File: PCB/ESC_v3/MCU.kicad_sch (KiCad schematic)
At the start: 44 parts, among them J10 Conn_01x01_Pin, J3 Conn_01x01_Pin, J4 Conn_01x01_Pin, J5 Conn_01x01_Pin, J6 Conn_01x01_Pin, J7 Conn_01x01_Pin, J8 Conn_01x01_Pin, J9 Conn_01x01_Pin, U5 STM32G431CBT6, Y2 24MHz

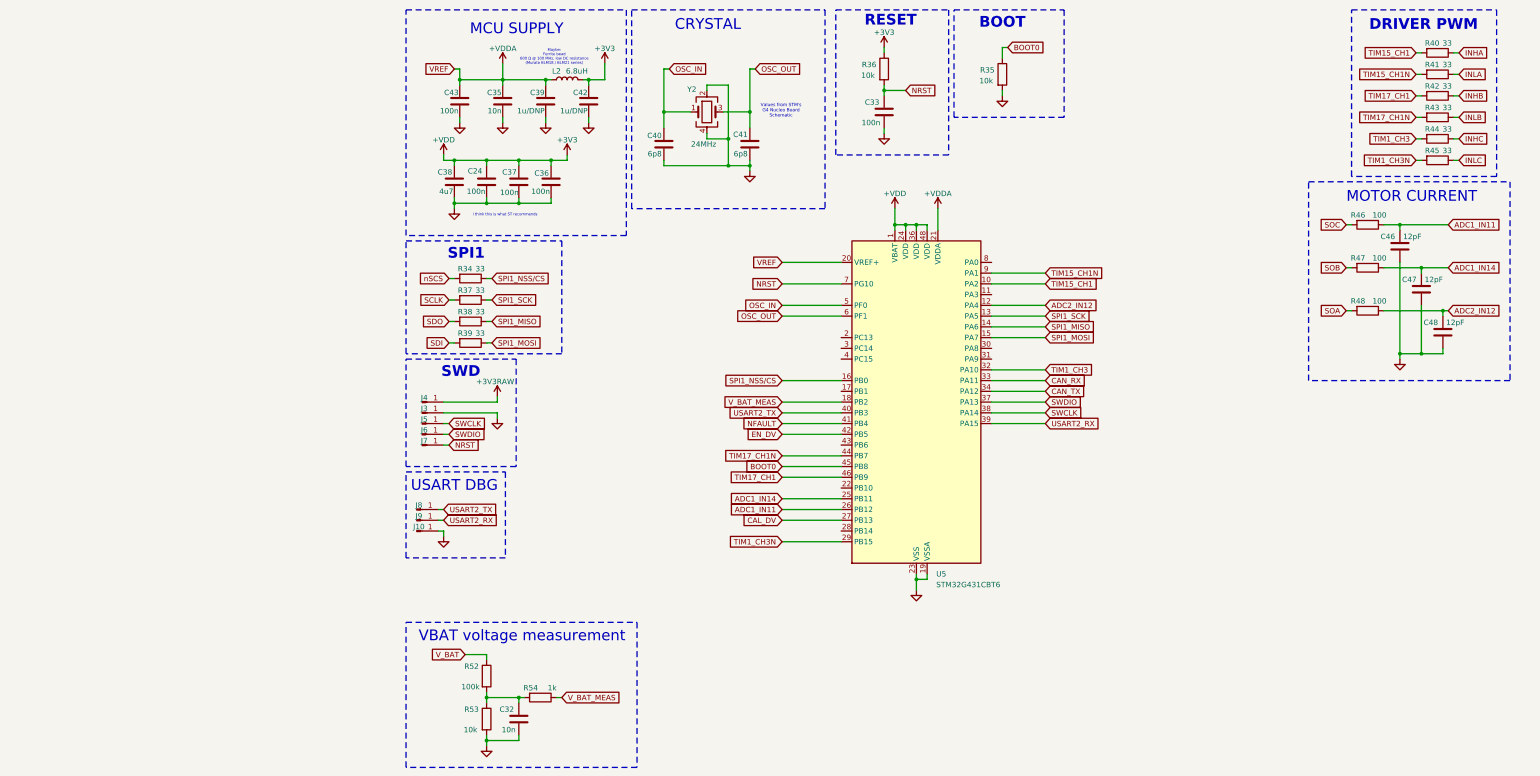
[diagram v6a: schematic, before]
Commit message: STM changed
Changed specific STM model for better pinouts and layout
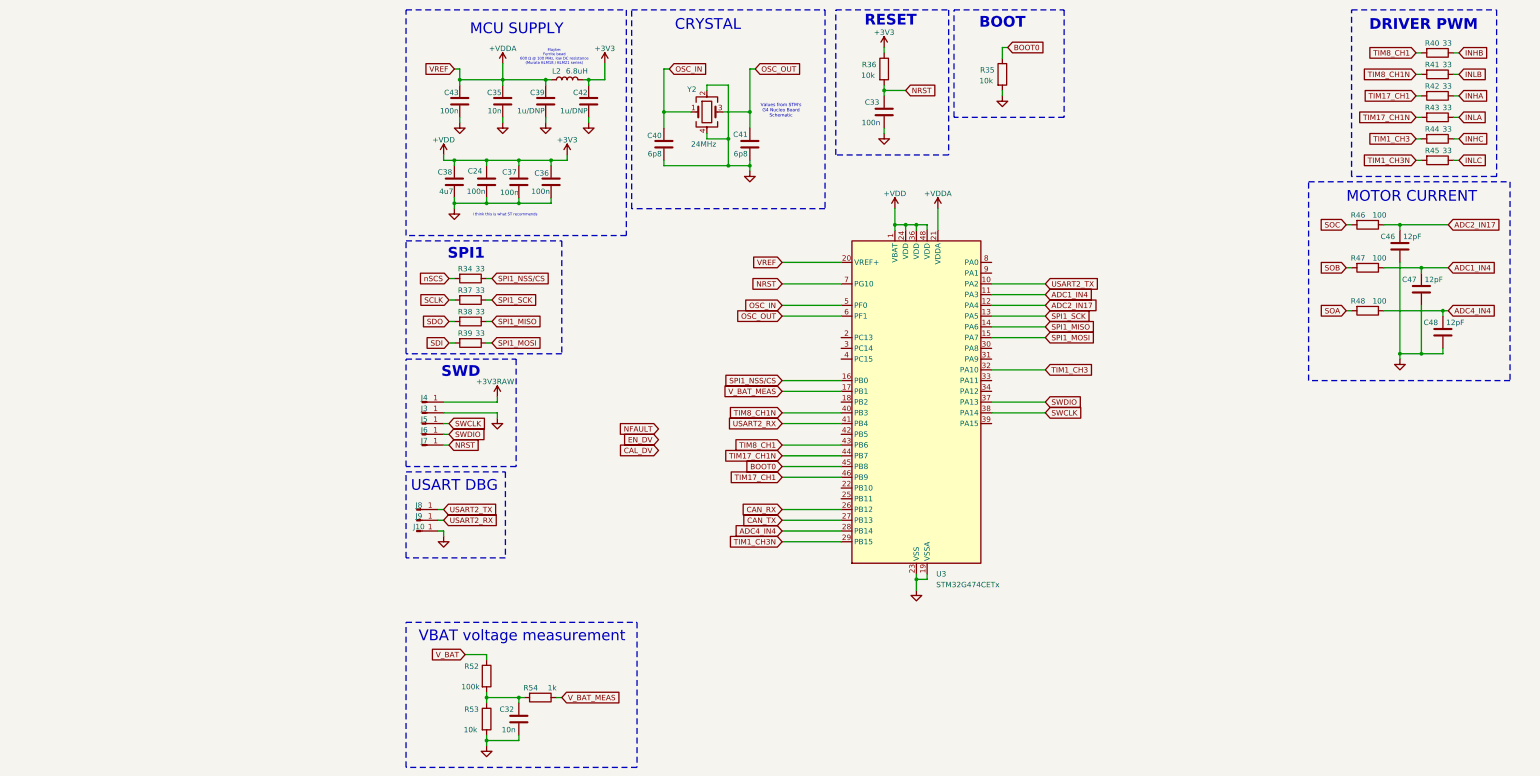
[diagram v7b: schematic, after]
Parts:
- removed U5: STM32G431CBT6, Package_QFP:LQFP-48_7x7mm_P0.5mm, symbol MCU_ST_STM32G4:STM32G431CBTx
- added U3: STM32G474CETx, Package_QFP:LQFP-48_7x7mm_P0.5mm, symbol MCU_ST_STM32G4:STM32G474CETx
- C35, C39, C42, C43, C46, C47: footprint Capacitor_SMD:C_0805_2012Metric -> Capacitor_SMD:C_0603_1608Metric
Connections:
- net +3V3: now also U3.1 (VBAT), U3.24 (VDD), U3.36 (VDD), U3.48 (VDD)
- net +VDDA: now also U3.20 (VREF+), U3.21 (VDDA)
- net BOOT0: now also U3.45 (PB8)
- net CAN_RX: now also U3.26 (PB12)
- net CAN_TX: now also U3.27 (PB13)
- net GND: now also U3.19 (VSSA), U3.23 (VSS), U3.35 (VSS), U3.47 (VSS)
- net INHA: now also R42.1; no longer R40.1
- net INHB: now also R40.1; no longer R42.1
- net INLA: now also R43.1; no longer R41.1
- net INLB: now also R41.1; no longer R43.1
- net NRST: now also U3.7 (PG10)
- net OSC_IN: now also U3.5 (PF0)
- net OSC_OUT: now also U3.6 (PF1)
- net SPI1_MISO: now also U3.14 (PA6)
- net SPI1_MOSI: now also U3.15 (PA7)
- net SPI1_NSS/CS: now also U3.16 (PB0)
- net SPI1_SCK: now also U3.13 (PA5)
- net SWCLK: now also U3.38 (PA14)
- net SWDIO: now also U3.37 (PA13)
- net TIM17_CH1: now also U3.46 (PB9)
- net TIM17_CH1N: now also U3.44 (PB7)
- net TIM1_CH3: now also U3.32 (PA10)
- net TIM1_CH3N: now also U3.29 (PB15)
- net USART2_RX: now also U3.41 (PB4)
- net USART2_TX: now also U3.10 (PA2)
- net V_BAT_MEAS: now also U3.17 (PB1)
- net ADC1_IN11 renamed ADC2_IN17
- net ADC2_IN17: now also U3.12 (PA4)
- net ADC1_IN14 renamed ADC1_IN4
- net ADC1_IN4: now also U3.11 (PA3)
- net ADC2_IN12 renamed ADC4_IN4
- net ADC4_IN4: now also U3.28 (PB14)
- net TIM15_CH1 renamed TIM8_CH1
- net TIM8_CH1: now also U3.43 (PB6)
- net TIM15_CH1N renamed TIM8_CH1N
- net TIM8_CH1N: now also U3.40 (PB3)

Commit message: Layout edit
Changed some layout and optimized
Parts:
- C24: footprint Capacitor_SMD:C_0805_2012Metric -> Capacitor_SMD:C_0603_1608Metric
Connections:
- net CAL_DV: now also U3.39 (PA15)
- net EN_DV: now also U3.34 (PA12)
- net nFAULT: now reaches U3.33 (PA11)
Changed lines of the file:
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@@
 	(wire
 		(pts
+			(xy 154.94 106.68) (xy 167.64 106.68)
+		)
+		(stroke
+			(width 0)
+			(type default)
+		)
+	)
+	(wire
+		(pts
 			(xy 137.16 67.31) (xy 137.16 68.58)
 		)
@@
 	(wire
 		(pts
+			(xy 167.64 104.14) (xy 154.94 104.14)
+		)
+		(stroke
+			(width 0)
+			(type default)
+		)
+	)
+	(wire
+		(pts
 			(xy 92.71 46.99) (xy 92.71 53.34)
 		)
@@
 	(wire
 		(pts
+			(xy 154.94 114.3) (xy 167.64 114.3)
+		)
+		(stroke
+			(width 0)
+			(type default)
+		)
+	)
+	(wire
+		(pts
 			(xy 167.64 101.6) (xy 154.94 101.6)
 		)
@@
 		)
 	)
+	(global_label "CAL_DV"
+		(shape input)
+		(at 167.64 114.3 0)
+		(fields_autoplaced yes)
+		(effects
+			(font
+				(size 1.27 1.27)
+				(thickness 0.1588)
+			)
+			(justify left)
+		)
+		(property "Intersheetrefs" "${INTERSHEET_REFS}"
+			(at 177.3381 114.3 0)
+			(effects
+				(font
+					(size 1.27 1.27)
+				)
+				(justify left)
+				(hide yes)
+			)
+		)
+	)
 	(global_label "EN_DV"
 		(shape input)
@@
 		)
 	)
+	(global_label "nFAULT"
+		(shape input)
+		(at 167.64 104.14 0)
+		(fields_autoplaced yes)
+		(effects
+			(font
+				(size 1.27 1.27)
+				(thickness 0.1588)
+			)
+			(justify left)
+		)
+		(property "Intersheetrefs" "${INTERSHEET_REFS}"
+			(at 177.7536 104.14 0)
+			(effects
+				(font
+					(size 1.27 1.27)
+				)
+				(justify left)
+				(hide yes)
+			)
+		)
+	)
 	(global_label "ADC2_IN17"
 		(shape input)
@@
 		)
 	)
+	(global_label "EN_DV"
+		(shape input)
+		(at 167.64 106.68 0)
+		(fields_autoplaced yes)
+		(effects
+			(font
+				(size 1.27 1.27)
+				(thickness 0.1588)
+			)
+			(justify left)
+		)
+		(property "Intersheetrefs" "${INTERSHEET_REFS}"
+			(at 176.4309 106.68 0)
+			(effects
+				(font
+					(size 1.27 1.27)
+				)
+				(justify left)
+				(hide yes)
+			)
+		)
+	)
 	(global_label "INHA"
 		(shape input)
@@
 			)
 		)
-		(property "Footprint" "Capacitor_SMD:C_0805_2012Metric"
+		(property "Footprint" "Capacitor_SMD:C_0603_1608Metric"
 			(at 34.5948 53.34 0)
 			(effects
